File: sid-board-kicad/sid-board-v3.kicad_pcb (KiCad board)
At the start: 2 copper layers, 60.1 x 60.1 mm, 49 parts, among them J1 SPI, J2 UART, J3 Conn_01x08, Q1 BSS138, SW1 BOOT, SW2 FLASH, U1 SC16IS752, U2 MCP1703A-3302, U3 SN65HVD232 x3, U4 SN65HVD232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

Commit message: Organisation and added more details
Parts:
- removed C3: 1uF, Capacitor_SMD:C_0805_2012Metric_Pad1.15x1.40mm_HandSolder
- added C8: 1uF, Capacitor_SMD:C_0805_2012Metric_Pad1.15x1.40mm_HandSolder, B.Cu at (134.5, 90.9)
- U2: value MCP1703A-3302 -> MCP1703A3302
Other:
- board text added: "IO"
- board text added: "MCP1703A 3302"

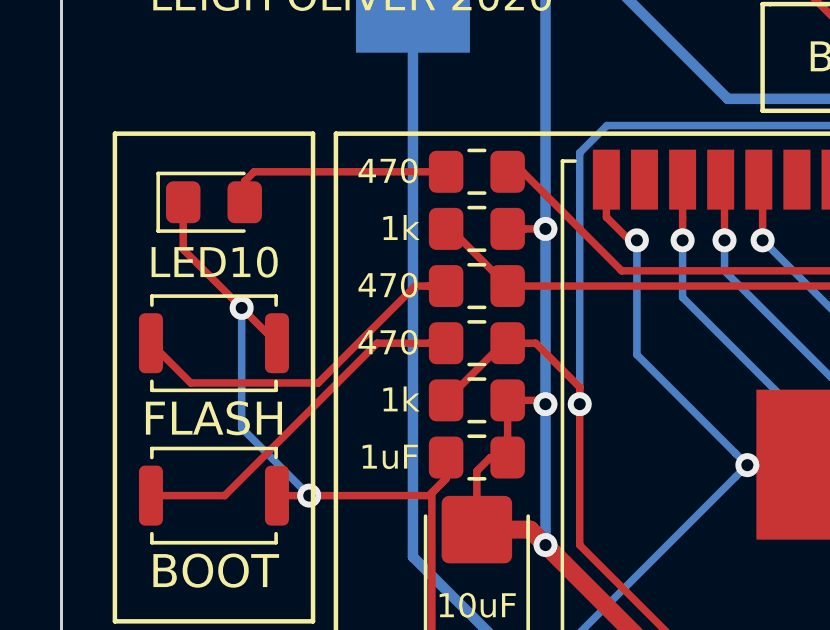
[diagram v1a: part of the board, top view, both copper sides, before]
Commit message: Added 10ks
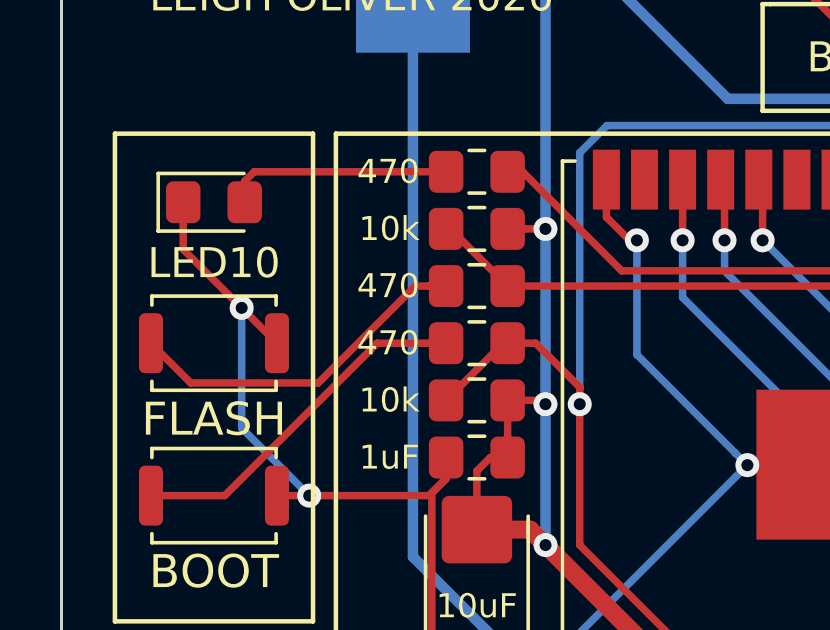
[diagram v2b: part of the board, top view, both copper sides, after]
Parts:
- R4, R5: value 1k -> 10k
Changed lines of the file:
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@@
       (effects (font (size 1 1) (thickness 0.15)) (justify right))
     )
-    (fp_text value 1k (at 1.905 0) (layer F.SilkS)
+    (fp_text value 10k (at 1.905 0) (layer F.SilkS)
       (effects (font (size 0.8 0.8) (thickness 0.2)) (justify right))
     )
@@
       (effects (font (size 1 1) (thickness 0.15)) (justify right))
     )
-    (fp_text value 1k (at 1.905 0) (layer F.SilkS)
+    (fp_text value 10k (at 1.905 0) (layer F.SilkS)
       (effects (font (size 0.8 0.8) (thickness 0.2)) (justify right))
     )
